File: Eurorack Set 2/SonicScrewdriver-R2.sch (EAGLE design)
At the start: 68 parts, among them IC1 LD1117AS33TR, IC2 MCP6004, IC3 LD1117AS33TR, IC4 7905, Q2 MMBT3904, U1 MKL02Z32VFK4, X1 CRYSTAL-0500290P1

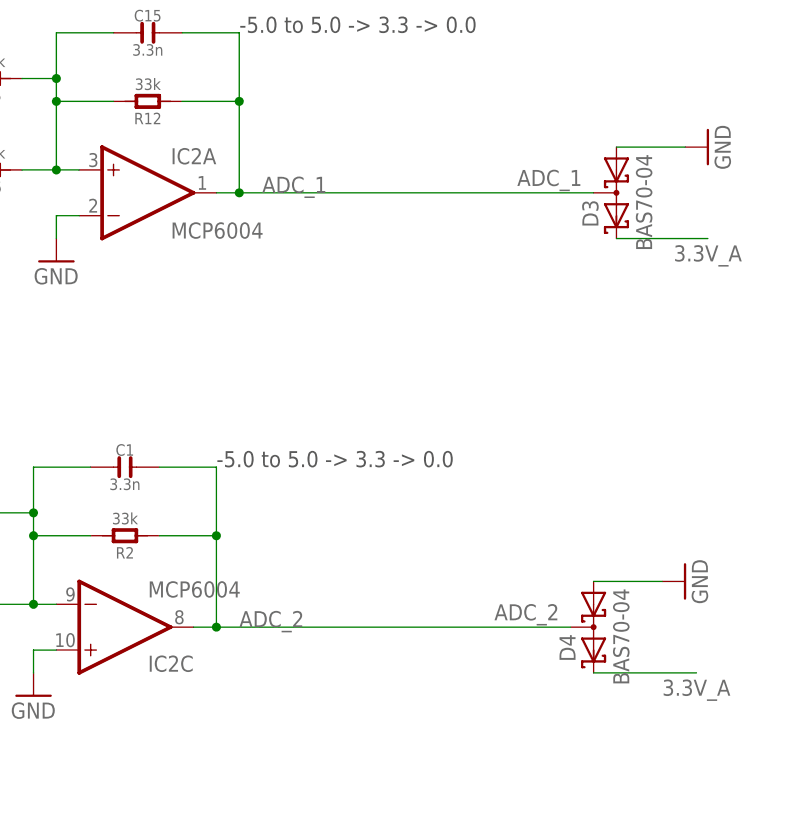
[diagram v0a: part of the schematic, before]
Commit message: More bodges - -12v line on fishfront, leds reversal, protection resistors on sonicscrewdriver
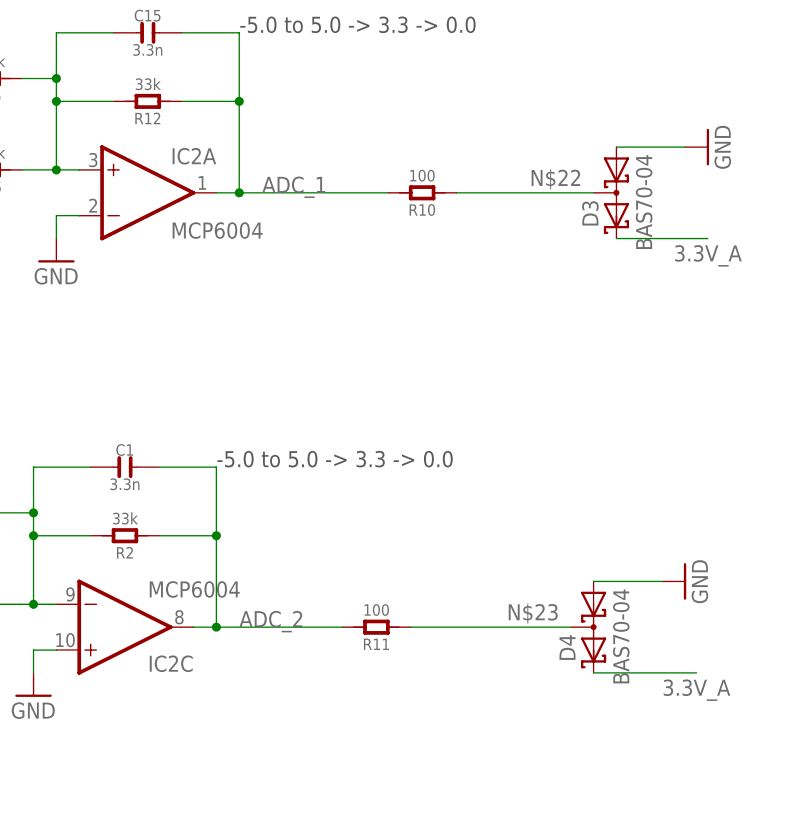
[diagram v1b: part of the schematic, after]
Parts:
- added R10, R11: 100, OPL:R-0603
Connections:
- new net N$22: D3.C1A2, R10.1
- new net N$23: D4.C1A2, R11.1
- net ADC_1: now also R10.2; no longer D3.C1A2
- net ADC_2: now also R11.2; no longer D4.C1A2
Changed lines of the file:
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@@
 <part name="GND44" library="SparkFun-Aesthetics" deviceset="GND" device=""/>
 <part name="GND45" library="SparkFun-Aesthetics" deviceset="GND" device=""/>
+<part name="R10" library="OPL" deviceset="R*" device="-0603" value="100"/>
+<part name="R11" library="OPL" deviceset="R*" device="-0603" value="100"/>
 </parts>
 <sheets>
@@
 <instance part="GND44" gate="1" x="113.03" y="-19.05" rot="R180"/>
 <instance part="GND45" gate="1" x="127" y="-16.51" rot="R180"/>
+<instance part="R10" gate="R" x="195.58" y="-71.12" rot="R180"/>
+<instance part="R11" gate="R" x="190.5" y="-119.38" rot="R180"/>
 </instances>
 <busses>
@@
 <pinref part="IC2" gate="C" pin="OUT"/>
 <pinref part="C1" gate="C" pin="2"/>
-<label x="210.82" y="-116.84" size="1.778" layer="95" rot="R180"/>
-<pinref part="D4" gate="G$1" pin="C1A2"/>
-<wire x1="172.72" y1="-119.38" x2="212.09" y2="-119.38" width="0.1524" layer="91"/>
+<wire x1="172.72" y1="-119.38" x2="186.69" y2="-119.38" width="0.1524" layer="91"/>
+<pinref part="R11" gate="R" pin="2"/>
 </segment>
 <segment>
@@
 <pinref part="C15" gate="C" pin="2"/>
 <pinref part="IC2" gate="A" pin="OUT"/>
-<label x="213.36" y="-68.58" size="1.778" layer="95" rot="R180"/>
-<pinref part="D3" gate="G$1" pin="C1A2"/>
-<wire x1="175.26" y1="-71.12" x2="214.63" y2="-71.12" width="0.1524" layer="91"/>
+<wire x1="175.26" y1="-71.12" x2="191.77" y2="-71.12" width="0.1524" layer="91"/>
+<pinref part="R10" gate="R" pin="2"/>
 </segment>
 <segment>
@@
 </segment>
 </net>
+<net name="N$22" class="0">
+<segment>
+<pinref part="D3" gate="G$1" pin="C1A2"/>
+<pinref part="R10" gate="R" pin="1"/>
+<wire x1="199.39" y1="-71.12" x2="214.63" y2="-71.12" width="0.1524" layer="91"/>
+<label x="213.36" y="-68.58" size="1.778" layer="95" rot="R180"/>
+</segment>
+</net>
+<net name="N$23" class="0">
+<segment>
+<pinref part="D4" gate="G$1" pin="C1A2"/>
+<pinref part="R11" gate="R" pin="1"/>
+<wire x1="194.31" y1="-119.38" x2="212.09" y2="-119.38" width="0.1524" layer="91"/>
+<label x="210.82" y="-116.84" size="1.778" layer="95" rot="R180"/>
+</segment>
+</net>

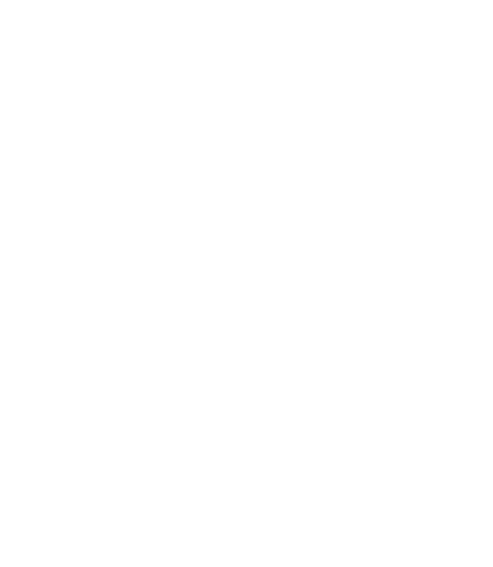
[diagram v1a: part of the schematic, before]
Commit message: Fiducials!
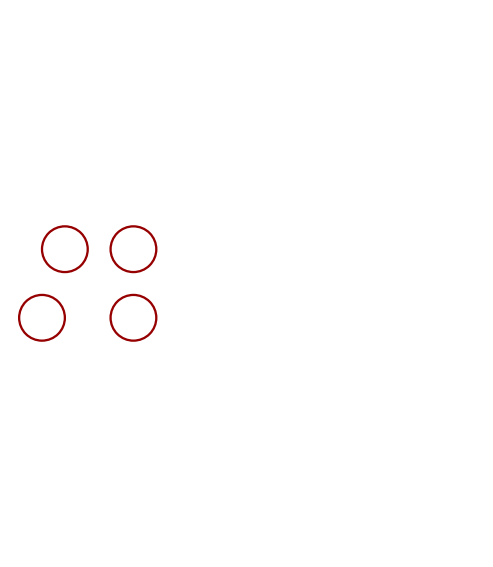
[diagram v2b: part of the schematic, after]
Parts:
- added U$11, U$4, U$5, U$9: FIDUCIAL, adafruit:FIDUCIAL
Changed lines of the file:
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@@
 <part name="R10" library="OPL" deviceset="R*" device="-0603" value="100"/>
 <part name="R11" library="OPL" deviceset="R*" device="-0603" value="100"/>
+<part name="U$4" library="adafruit" deviceset="FIDUCIAL" device=""/>
+<part name="U$5" library="adafruit" deviceset="FIDUCIAL" device=""/>
+<part name="U$9" library="adafruit" deviceset="FIDUCIAL" device=""/>
+<part name="U$11" library="adafruit" deviceset="FIDUCIAL" device=""/>
 </parts>
 <sheets>
@@
 <instance part="R10" gate="R" x="195.58" y="-71.12" rot="R180"/>
 <instance part="R11" gate="R" x="190.5" y="-119.38" rot="R180"/>
+<instance part="U$4" gate="G$1" x="-38.1" y="71.12"/>
+<instance part="U$5" gate="G$1" x="-30.48" y="71.12"/>
+<instance part="U$9" gate="G$1" x="-30.48" y="63.5"/>
+<instance part="U$11" gate="G$1" x="-40.64" y="63.5"/>
 </instances>
 <busses>
